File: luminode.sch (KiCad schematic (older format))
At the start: 4 parts

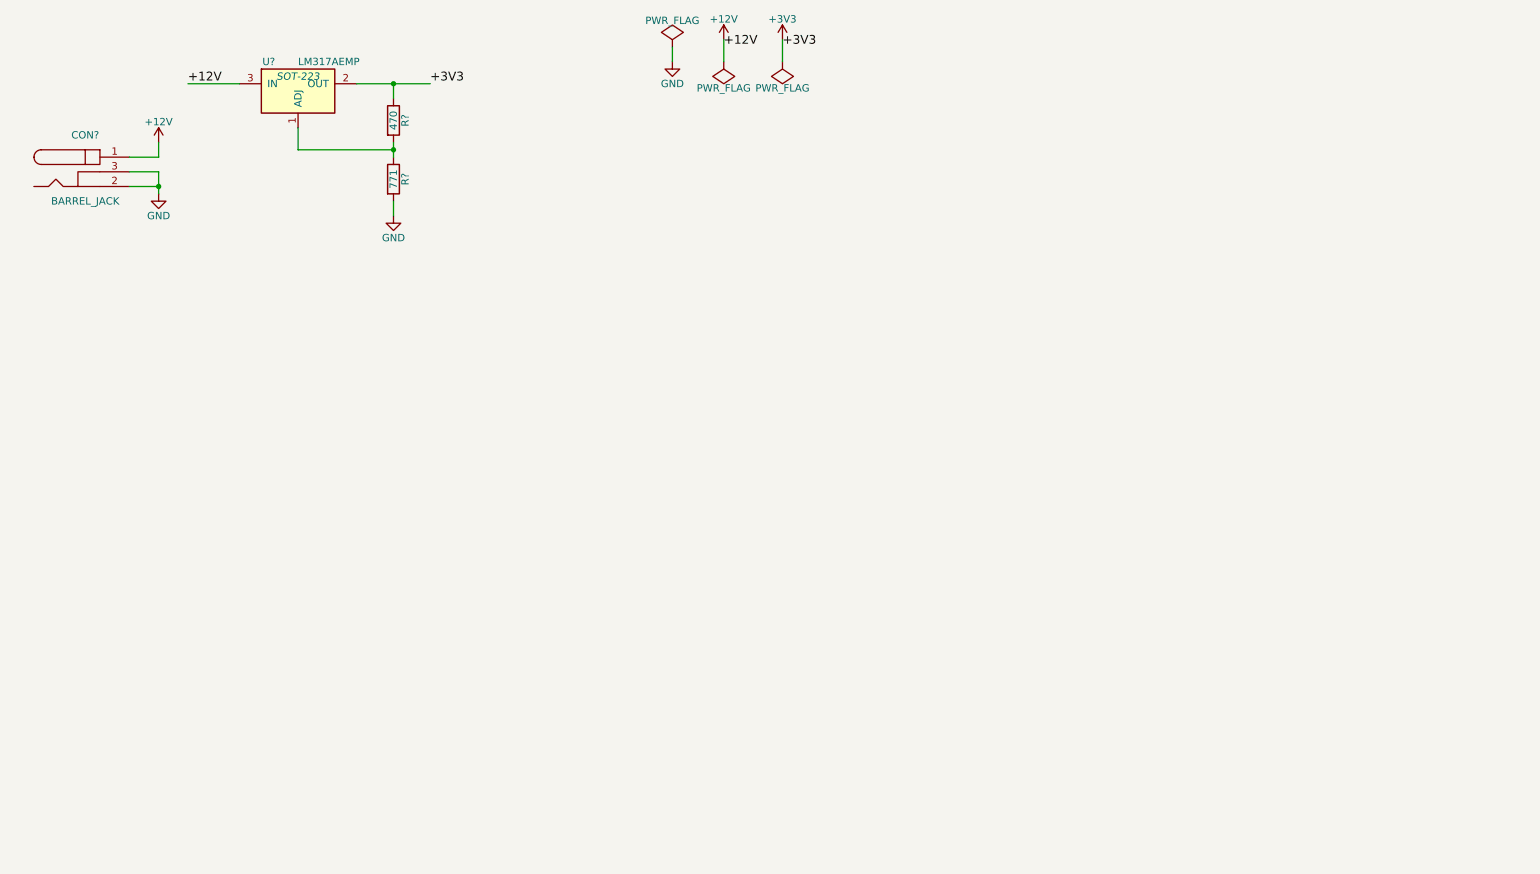
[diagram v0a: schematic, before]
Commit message: gpio configuration and flashing
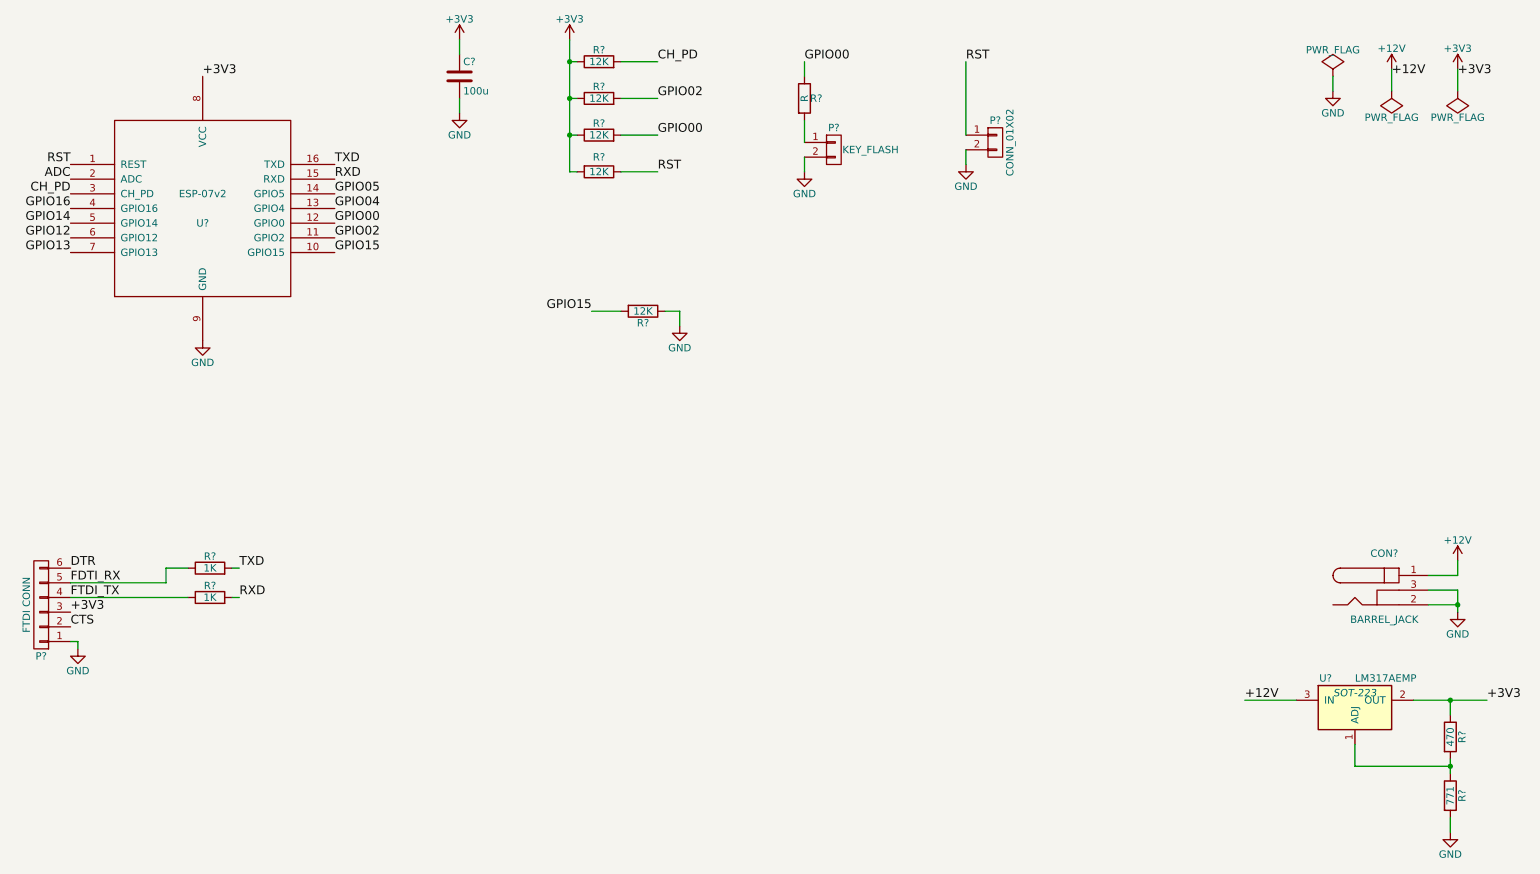
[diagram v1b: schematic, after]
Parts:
- added C?: 100u, symbol C
- added P?: CONN_01X02, symbol CONN_01X02
- added P?: FTDI CONN, symbol CONN_01X06
- added P?: KEY_FLASH, symbol CONN_01X02
- added R? (x5): 12K, symbol R
- added R? (x2): 1K, symbol R
- added R?: R, symbol R
- added U?: ESP-07v2, symbol ESP-07v2
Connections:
- net +3V3: now also C?.1, P?.3 (P3), R?.1, R?.1, R?.1, R?.2, U?.8 (VCC)
- net GND: now also C?.2, P?.1 (P1), P?.2 (P2), P?.2 (P2), R?.1, U?.9 (GND)
- new net: P?.1 (P1), R?.2
- new net ADC: U?.2 (ADC)
- new net CH_PD: R?.2, U?.3 (CH_PD)
- new net CTS: P?.2 (P2)
- new net DTR: P?.6 (P6)
- new net FDTI_RX: P?.5 (P5), R?.1
- new net FTDI_TX: P?.4 (P4), R?.1
- new net GPIO00: R?.1, R?.2, U?.12 (GPIO0)
- new net GPIO02: R?.2, U?.11 (GPIO2)
- new net GPIO04: U?.13 (GPIO4)
- new net GPIO05: U?.14 (GPIO5)
- new net GPIO12: U?.6 (GPIO12)
- new net GPIO13: U?.7 (GPIO13)
- new net GPIO14: U?.5 (GPIO14)
- new net GPIO15: R?.2, U?.10 (GPIO15)
- new net GPIO16: U?.4 (GPIO16)
- new net RST: P?.1 (P1), R?.1, U?.1 (REST)
- new net RXD: R?.2, U?.15 (RXD)
- new net TXD: R?.2, U?.16 (TXD)
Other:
- moved on the sheet: CON?, R?, U?
